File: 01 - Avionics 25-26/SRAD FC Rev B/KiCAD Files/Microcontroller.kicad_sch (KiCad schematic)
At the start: 4 parts

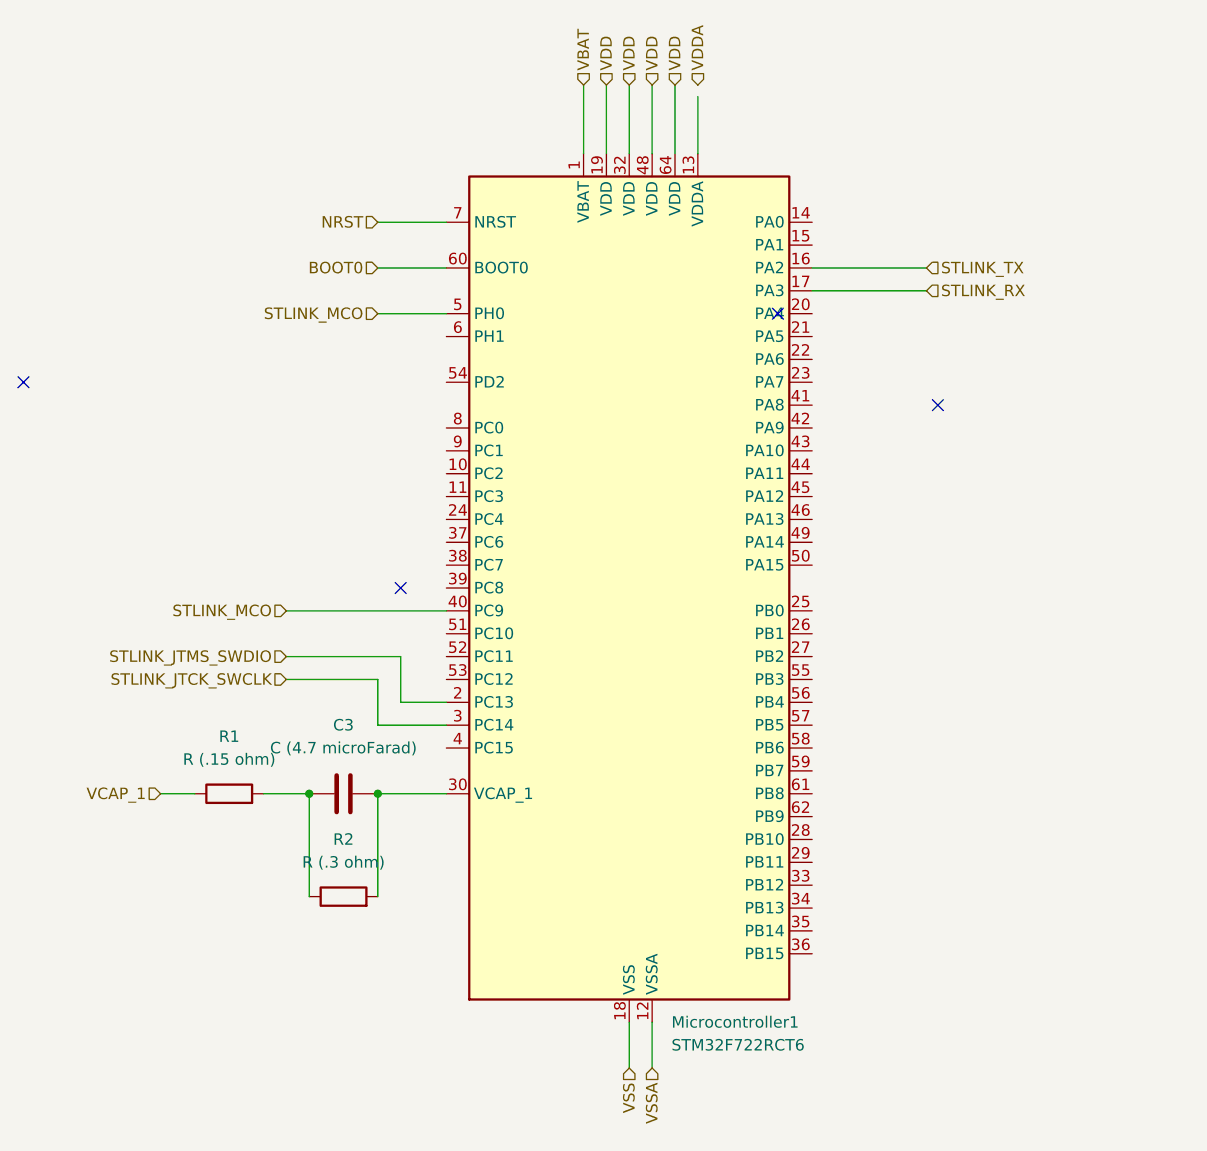
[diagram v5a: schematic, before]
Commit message: removed unneccessary debug wires
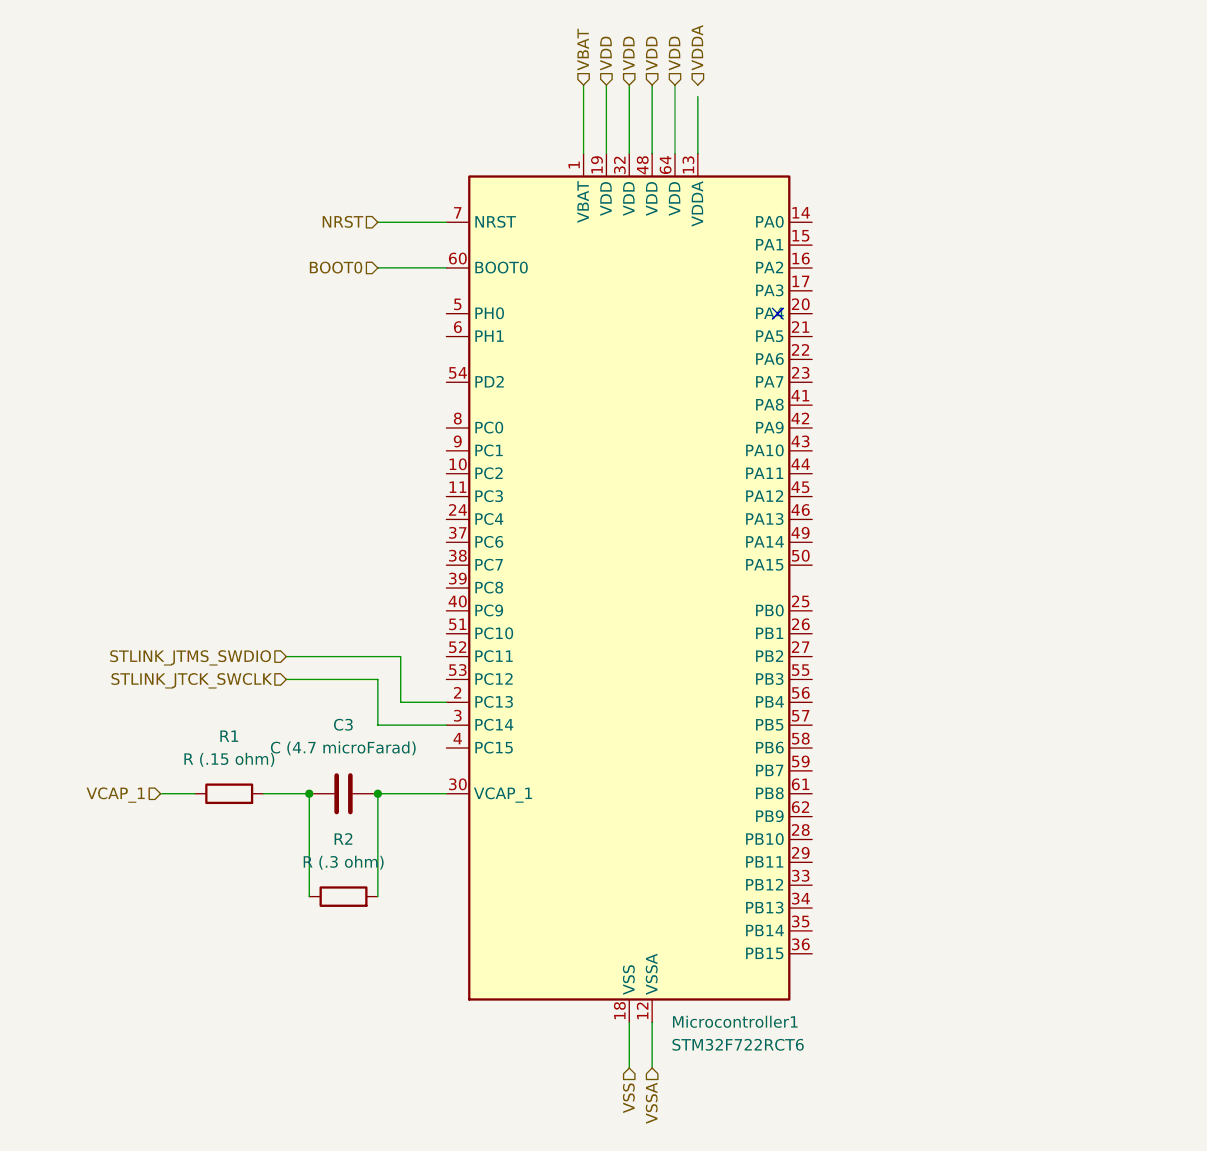
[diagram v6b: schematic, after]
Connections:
- net STLINK_MCO: no longer names the net of Microcontroller1.40 (PC9)
- net STLINK_MCO: no longer Microcontroller1.5 (PH0)
- net STLINK_RX: no longer names the net of Microcontroller1.17 (PA3)
- net STLINK_TX: no longer names the net of Microcontroller1.16 (PA2)
- no-connect marks 4 -> 1
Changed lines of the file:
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@@
-	)
-	(no_connect
-		(at 154.94 73.66)
-	)
-	(no_connect
-		(at 95.25 93.98)
 	)
 	(no_connect
 		(at 137.16 63.5)
 	)
-	(no_connect
-		(at 53.34 71.12)
-	)
-	(wire
-		(pts
-			(xy 82.55 96.52) (xy 100.33 96.52)
-		)
-		(stroke
-			(width 0)
-			(type default)
-		)
-	)
 	(wire
 		(pts
@@
 	(wire
 		(pts
-			(xy 140.97 60.96) (xy 153.67 60.96)
-		)
-		(stroke
-			(width 0)
-			(type default)
-		)
-	)
-	(wire
-		(pts
 			(xy 120.65 38.1) (xy 120.65 45.72)
 		)
@@
 	(wire
 		(pts
-			(xy 140.97 58.42) (xy 153.67 58.42)
-		)
-		(stroke
-			(width 0)
-			(type default)
-		)
-	)
-	(wire
-		(pts
 			(xy 95.25 106.68) (xy 100.33 106.68)
 		)
@@
 	(wire
 		(pts
-			(xy 92.71 63.5) (xy 100.33 63.5)
-		)
-		(stroke
-			(width 0)
-			(type default)
-		)
-	)
-	(wire
-		(pts
 			(xy 100.33 109.22) (xy 92.71 109.22)
 		)
@@
 		)
 	)
-	(hierarchical_label "STLINK_RX"
-		(shape input)
-		(at 153.67 60.96 0)
-		(effects
-			(font
-				(size 1.27 1.27)
-			)
-			(justify left)
-		)
-	)
-	(hierarchical_label "STLINK_MCO"
-		(shape input)
-		(at 92.71 63.5 180)
-		(effects
-			(font
-				(size 1.27 1.27)
-			)
-			(justify right)
-		)
-	)
 	(hierarchical_label "STLINK_JTMS_SWDIO"
 		(shape input)
@@
 		)
 	)
-	(hierarchical_label "STLINK_TX"
-		(shape input)
-		(at 153.67 58.42 0)
-		(effects
-			(font
-				(size 1.27 1.27)
-			)
-			(justify left)
-		)
-	)
 	(hierarchical_label "VDD"
 		(shape input)
@@
 		(effects
 			(font
-				(size 1.27 1.27)
-			)
-			(justify right)
-		)
-	)
-	(hierarchical_label "STLINK_MCO"
-		(shape input)
-		(at 82.55 96.52 180)
-		(effects
-			(font

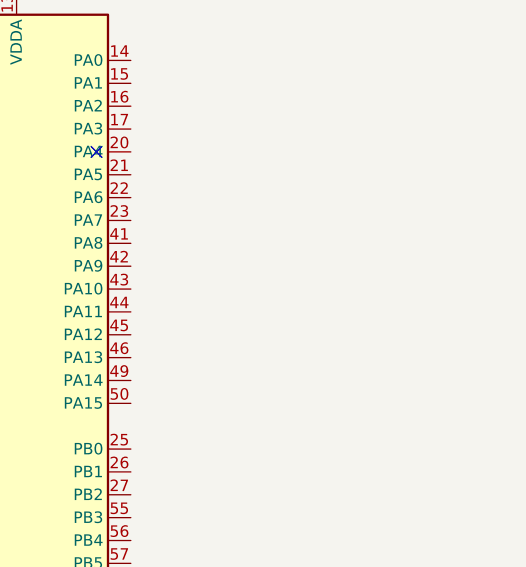
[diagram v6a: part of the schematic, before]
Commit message: wired spi bus in top level sheet
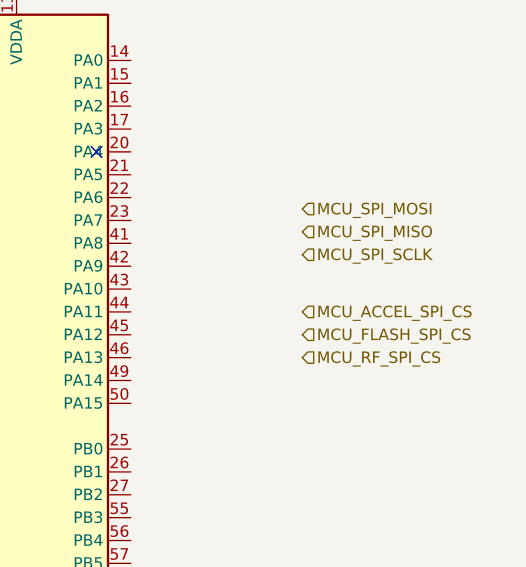
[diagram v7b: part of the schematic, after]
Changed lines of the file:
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@@
+		)
+	)
+	(hierarchical_label "MCU_FLASH_SPI_CS"
+		(shape input)
+		(at 160.02 83.82 0)
+		(effects
+			(font
+				(size 1.27 1.27)
+			)
+			(justify left)
 		)
 	)
@@
 		)
 	)
+	(hierarchical_label "MCU_RF_SPI_CS"
+		(shape input)
+		(at 160.02 86.36 0)
+		(effects
+			(font
+				(size 1.27 1.27)
+			)
+			(justify left)
+		)
+	)
 	(hierarchical_label "VDD"
 		(shape input)
@@
 		)
 	)
+	(hierarchical_label "MCU_SPI_SCLK"
+		(shape input)
+		(at 160.02 74.93 0)
+		(effects
+			(font
+				(size 1.27 1.27)
+			)
+			(justify left)
+		)
+	)
 	(hierarchical_label "VCAP_1"
 		(shape input)
@@
 		(effects
 			(font
+				(size 1.27 1.27)
+			)
+			(justify left)
+		)
+	)
+	(hierarchical_label "MCU_SPI_MISO"
+		(shape input)
+		(at 160.02 72.39 0)
+		(effects
+			(font
+				(size 1.27 1.27)
+			)
+			(justify left)
+		)
+	)
+	(hierarchical_label "MCU_ACCEL_SPI_CS"
+		(shape input)
+		(at 160.02 81.28 0)
+		(effects
+			(font
+				(size 1.27 1.27)
+			)
+			(justify left)
+		)
+	)
+	(hierarchical_label "MCU_SPI_MOSI"
+		(shape input)
+		(at 160.02 69.85 0)
+		(effects
+			(font

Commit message: continued wiring spi bus
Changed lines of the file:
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@@
+		)
+	)
+	(hierarchical_label "MCU_BARO_SPI_CS"
+		(shape input)
+		(at 160.02 88.9 0)
+		(effects
+			(font
+				(size 1.27 1.27)
+			)
+			(justify left)
 		)
 	)
@@
 		(effects
 			(font
+				(size 1.27 1.27)
+			)
+			(justify left)
+		)
+	)
+	(hierarchical_label "MCU_IMU_SPI_CS"
+		(shape input)
+		(at 160.02 91.44 0)
+		(effects
+			(font
